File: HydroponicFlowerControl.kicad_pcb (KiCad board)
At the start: 4 copper layers, 101 x 101 mm, 233 parts, among them IC1 ADM3260ARSZ-RL7, IC2 ADM3260ARSZ-RL7, IC3 CH224K, J1 EC, J10 Pump 1, J11 Temperature, J12 Pump 2, J13 Pump 3, J14 D IN1, J15 D IN2, J16 D IN3, J17 CAN, J18 Raspberry_Pi_2_3, J19 Conn_ARM_JTAG_SWD_10, J2 Temp, J20 Conn_ARM_JTAG_SWD_10, J3 Flow, J4 pH, J5 USB_C_Receptacle_USB2.0, J6 Barrel_Jack, J7 Valve 1, J8 Valve 2, J9 Valve 3, Q1 MMBT3904, Q10 AO3401A, Q11 MMBT3904, Q12 AO3401A, Q2 AO3401A, Q3 MMBT3904, Q4 AO3401A, Q5 MMBT3904, Q6 AO3401A, Q7 MMBT3904, Q8 MMBT3904, Q9 AO3401A, SW1 RESET, U10 REF3020, U11 TPS60400DBV, U12 ADS1115IDGS, U14 TLV271, U15 TLV271, U16 MCP2518FD-xQBB, U17 HDC1080, U18 SN65HVD230, U19 SN65HVD230, U2 ADS1115IDGS, U20 TPS5430DDA, U4 TPS60400DBV, U5 LM324, U6 MCP4017T-502E/LT, U7 LM358, U8 STM32G431CBTx, U9 AMS1117-3.3, Y1 8 MHz, Y2 40MHz

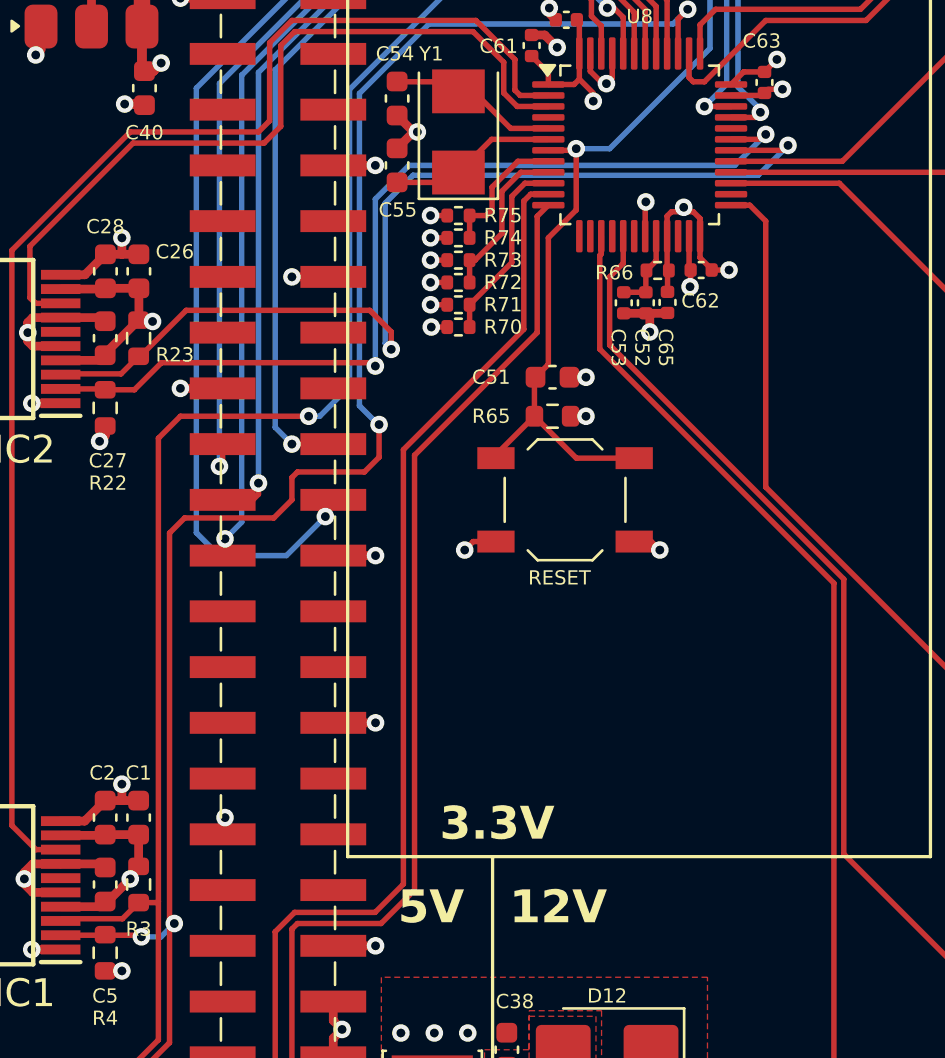
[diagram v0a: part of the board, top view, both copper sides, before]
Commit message: Add RPi ID EEPROM
Closes #15
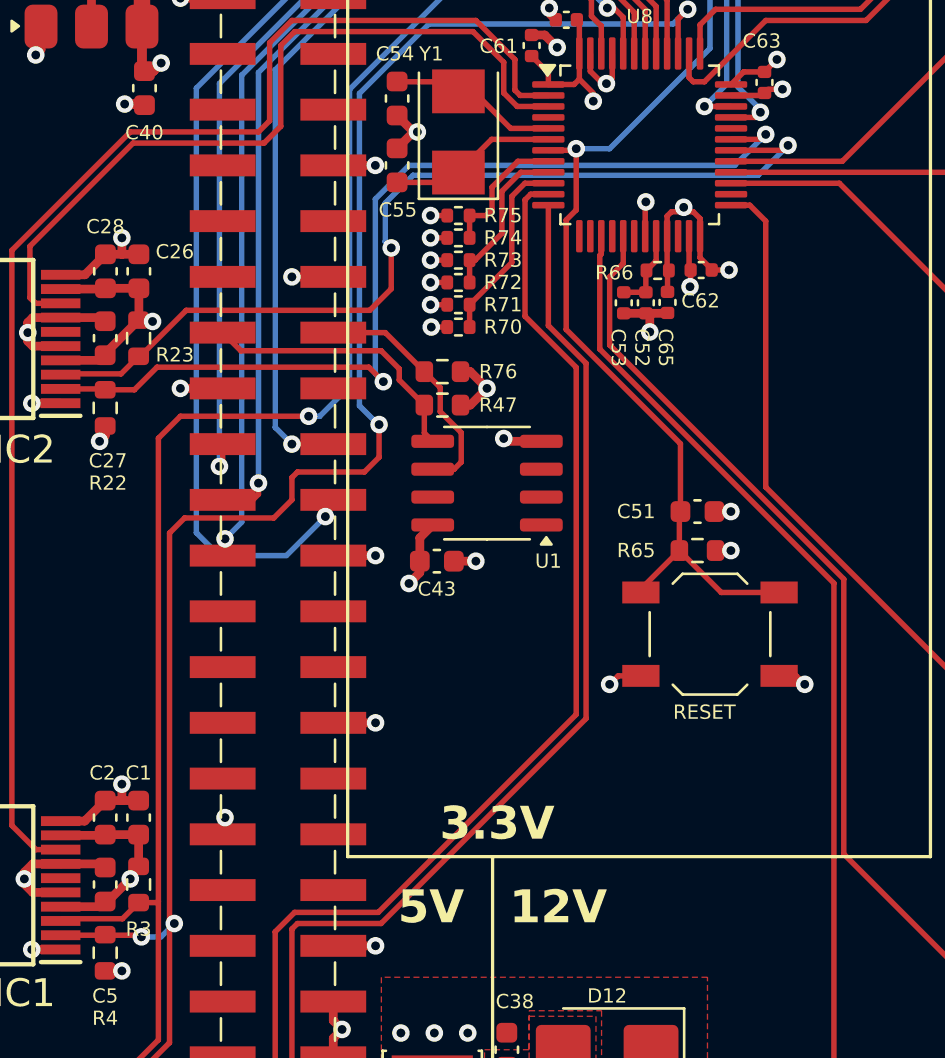
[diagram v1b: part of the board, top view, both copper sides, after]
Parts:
- added C43: 100nF/0.1uF, Capacitor_SMD:C_0603_1608Metric, F.Cu at (113.1, 106.4)
- added R47: 3.9k, Resistor_SMD:R_0603_1608Metric, F.Cu at (113.4, 99.2)
- added R76: 3.9k, Resistor_SMD:R_0603_1608Metric, F.Cu at (113.4, 97.7)
- added U1: AT24C256C, Package_SO:SOIC-8_3.9x4.9mm_P1.27mm, F.Cu at (115.4, 102.8)
- moved C51 9.00 mm to (125.0, 104.1)
- moved SW1 9.00 mm to (125.6, 109.7)
- moved R65 9.00 mm to (125.0, 105.9)
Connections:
- J18 pad 27: unconnected-(J18-ID_SD/GPIO0-Pad27) -> /RaspberryPi/ID_SDA
- J18 pad 28: unconnected-(J18-ID_SC/GPIO1-Pad28) -> /RaspberryPi/ID_SCL
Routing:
- net /RaspberryPi/ID_SDA: track 0.00 -> 12.7 mm
- net /RaspberryPi/ID_SCL: track 0.00 -> 11.1 mm
- net ~{RESET}: track 78.3 -> 86.0 mm
- net +3.3V: track 78.5 -> 84.6 mm, vias 19 -> 21
- net /MCU/I2C1_SDA: track 46.3 -> 42.7 mm
- net GND: track 151.6 -> 154.4 mm, vias 88 -> 90
- net /Flow control/FLOW: track 95.8 -> 97.8 mm
- net /Flow control/TEMP: track 89.8 -> 91.2 mm
- net /MCU/I2C1_SCL: track 43.2 -> 44.5 mm

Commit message: Switch to basic components for 5V LDO feedback
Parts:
- R68: value 10k -> 6.2k
- R69: value 3.24k -> 2k
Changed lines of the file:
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@@
 			)
 		)
-		(property "Value" "3.24k"
+		(property "Value" "2k"
 			(at 0 1.43 180)
 			(layer "F.Fab")
@@
 			)
 		)
-		(property "LCSC" "C22994"
+		(property "LCSC" "C22975"
 			(at 0 0 180)
 			(unlocked yes)
@@
 		(sheetname "Power")
 		(sheetfile "power.kicad_sch")
-		(attr smd exclude_from_pos_files exclude_from_bom)
+		(attr smd)
 		(fp_line
 			(start -0.237258 0.5225)
@@
 		(tags "SOIC SO")
 		(property "Reference" "U1"
-			(at -2.794 -3.556 360)
+			(at -2.794 -3.556 0)
 			(layer "F.SilkS")
 			(effects
@@
 		)
 		(property "Value" "AT24C256C"
-			(at 0 3.4 360)
+			(at 0 3.4 0)
 			(layer "F.Fab")
 			(effects
@@
 		)
 		(fp_text user "${REFERENCE}"
-			(at 0 0 360)
+			(at 0 0 0)
 			(layer "F.Fab")
 			(effects
@@
 		(tags "resistor")
 		(property "Reference" "R76"
-			(at -2.54 0 360)
+			(at -2.54 0 0)
 			(layer "F.SilkS")
 			(effects
@@
 		)
 		(property "Value" "3.9k"
-			(at 0 1.43 360)
+			(at 0 1.43 0)
 			(layer "F.Fab")
 			(effects
@@
 		)
 		(fp_text user "${REFERENCE}"
-			(at 0 0 360)
+			(at 0 0 0)
 			(layer "F.Fab")
 			(effects
@@
 		(tags "resistor")
 		(property "Reference" "R47"
-			(at -2.54 0 360)
+			(at -2.54 0 0)
 			(layer "F.SilkS")
 			(effects
@@
 		)
 		(property "Value" "3.9k"
-			(at 0 1.43 360)
+			(at 0 1.43 0)
 			(layer "F.Fab")
 			(effects
@@
 		)
 		(fp_text user "${REFERENCE}"
-			(at 0 0 360)
+			(at 0 0 0)
 			(layer "F.Fab")
 			(effects
@@
 			)
 		)
-		(property "Value" "10k"
+		(property "Value" "6.2k"
 			(at 0 1.43 180)
 			(layer "F.Fab")
@@
 			)
 		)
-		(property "LCSC" "C25804"
+		(property "LCSC" "C4260"
 			(at 0 0 180)
 			(unlocked yes)

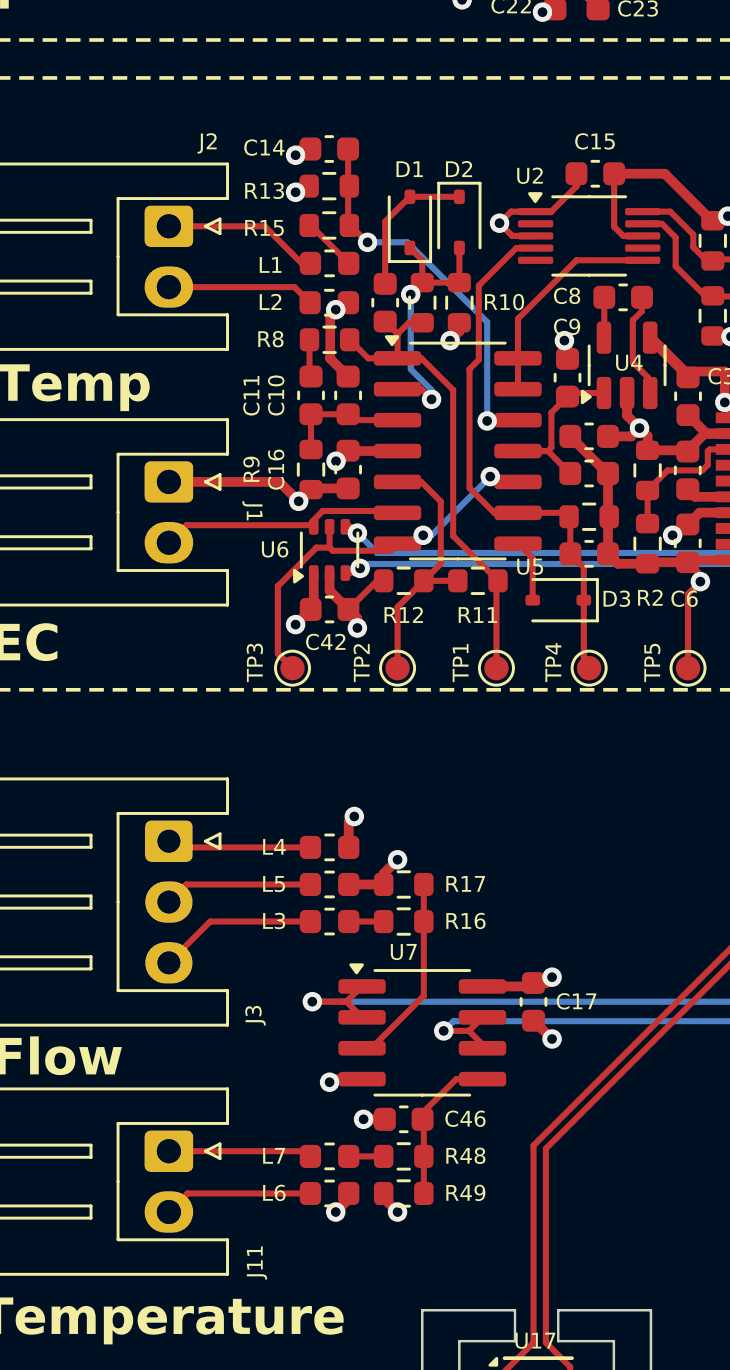
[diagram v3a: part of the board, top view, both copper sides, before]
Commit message: Move R15 and R48 to the right side of the divider
Closes #6
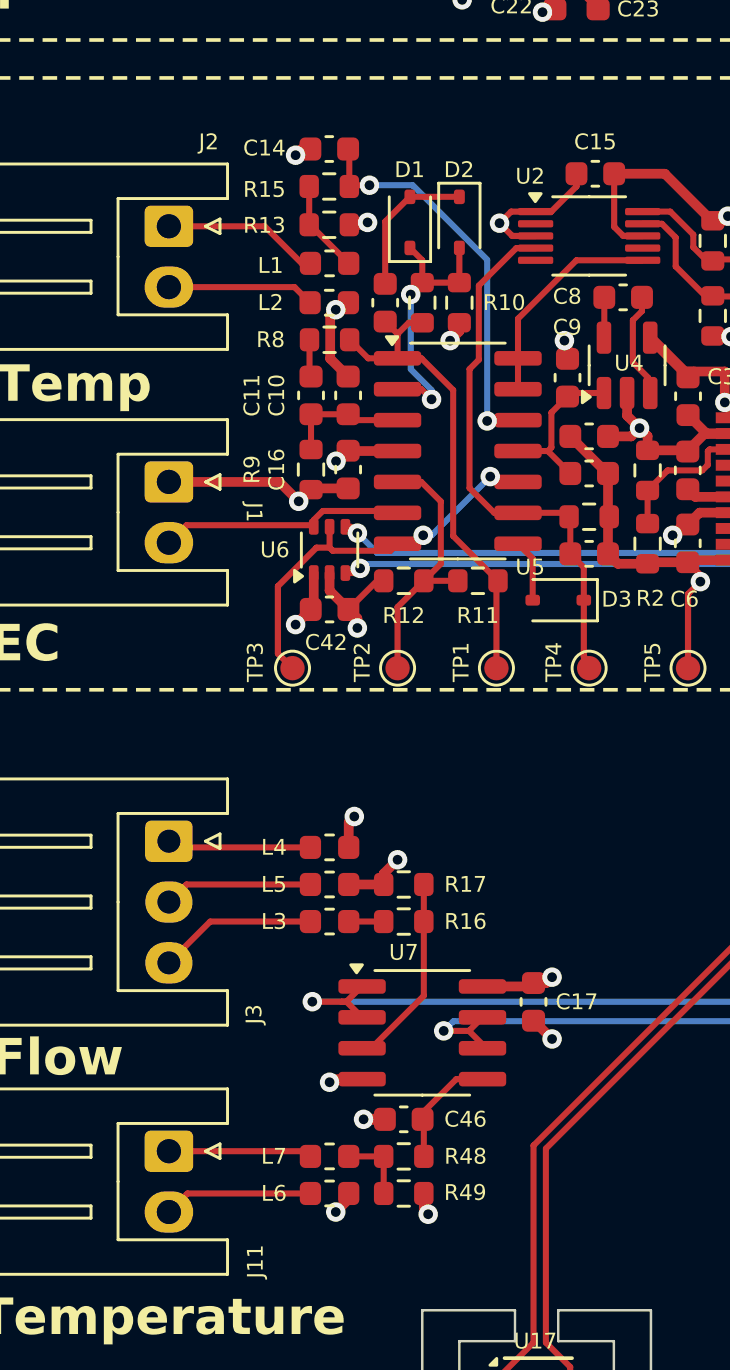
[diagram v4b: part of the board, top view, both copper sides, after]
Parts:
- moved R15 1.60 mm to (72.1, 108.7)
- moved R13 1.59 mm to (72.1, 110.3), turned to 180 degrees
- turned R49 to 180 degrees
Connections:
- R13 pad 2: Net-(U5D-+) -> Net-(L1-Pad2)
- R49 pad 2: Net-(U7B-+) -> Net-(L7-Pad2)
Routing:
- net Net-(L1-Pad2): track 2.20 -> 3.86 mm
- net Net-(L7-Pad2): track 1.44 -> 2.96 mm
- net Net-(U7B-+): track 6.03 -> 4.58 mm
- net Net-(U5D-+): track 15.7 -> 16.5 mm

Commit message: Optimize EC RC filter
Closes #5
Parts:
- C13: value 1uF -> 10uF; footprint Capacitor_SMD:C_0603_1608Metric -> Capacitor_SMD:C_0805_2012Metric
- R14: value 1k -> 10k
- moved D3 0.35 mm to (81.5, 126.0)
- moved R14 0.16 mm to (82.8, 122.1)
- moved R2 0.10 mm to (85.3, 123.4)
- moved C13 0.10 mm to (82.8, 123.9)
- moved R1 0.08 mm to (85.3, 120.4)

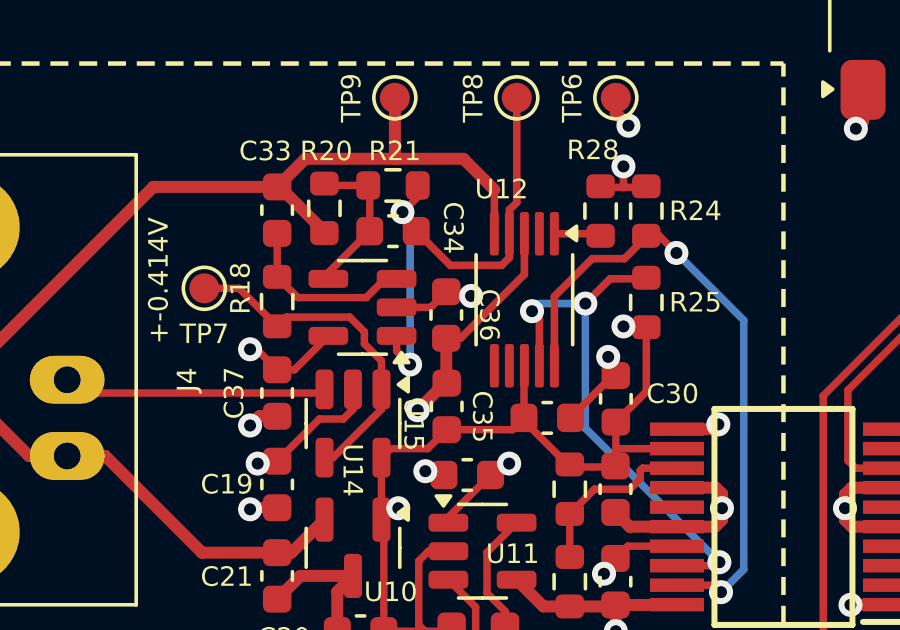
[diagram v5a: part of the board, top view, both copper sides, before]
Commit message: Protect PH_OUT from going out of bounds
Closes #7
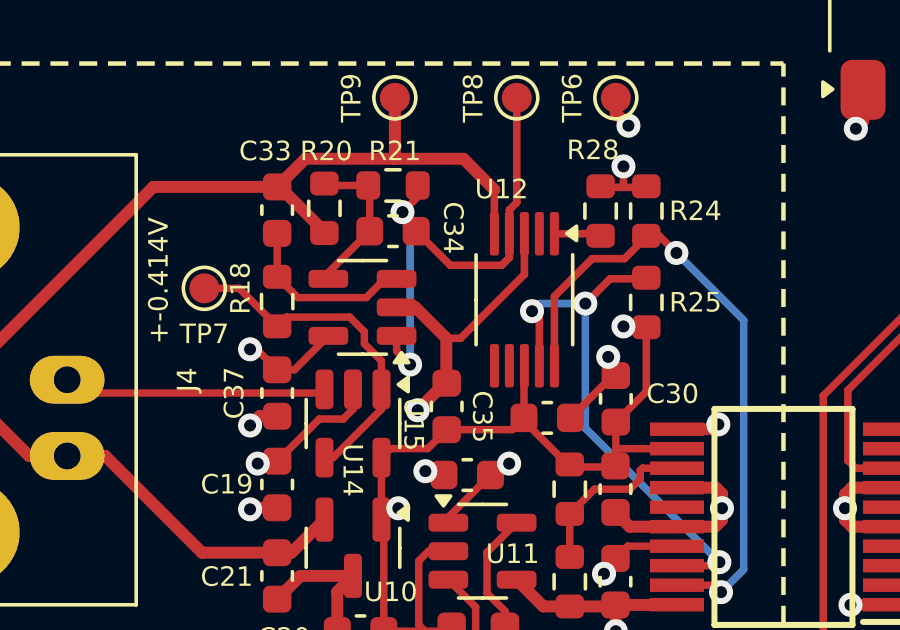
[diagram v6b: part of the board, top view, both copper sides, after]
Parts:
- removed C36: 100nF/0.1uF, Capacitor_SMD:C_0603_1608Metric
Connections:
- U14 pad 2: -5V_isoPH -> GND_iosPH
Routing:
- net -5V_isoPH: track 24.9 -> 16.1 mm, vias 3 -> 2
- net GND_iosPH: track 34.7 -> 36.8 mm
